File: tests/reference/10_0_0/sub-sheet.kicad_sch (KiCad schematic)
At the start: 1 part, among them U1 74LS04

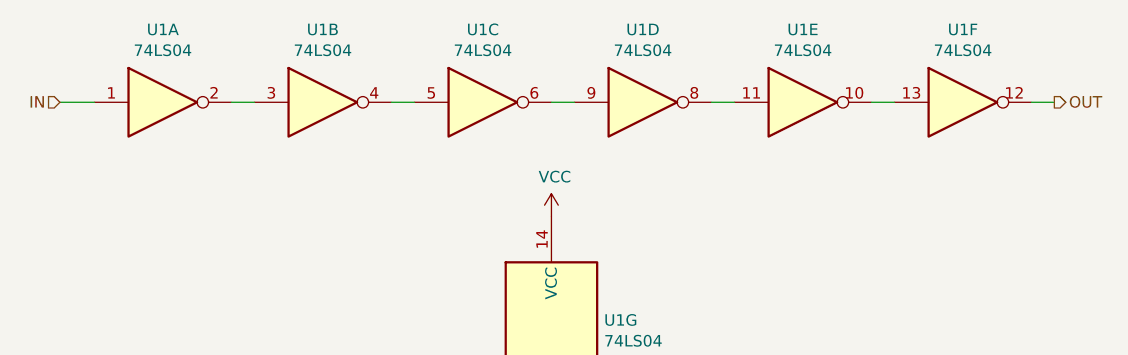
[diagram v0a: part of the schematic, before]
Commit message: [Schematic][Added] Support for private texts on symbols
- Introduced in KiCad 9
- Not documented, as usual
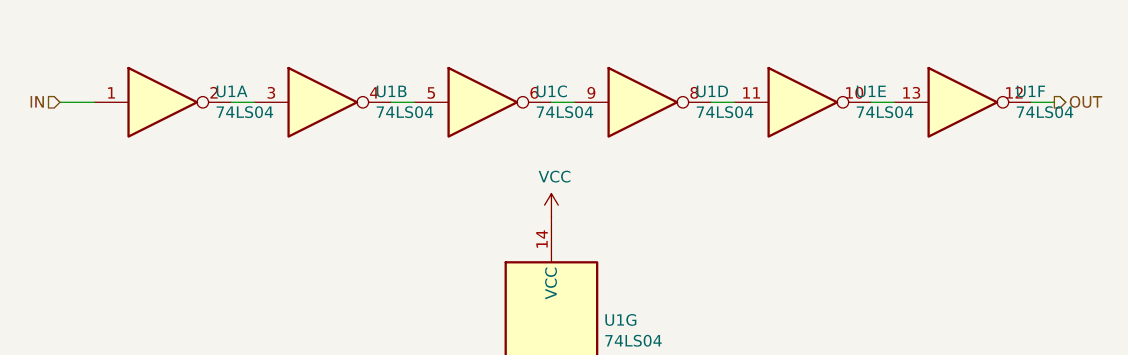
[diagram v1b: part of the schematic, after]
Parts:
- U1: private (none) -> PrivateField
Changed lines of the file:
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@@
-(kicad_sch (version 20260101) (generator "eeschema") (generator_version "10.0")
+(kicad_sch (version 20260306) (generator "eeschema") (generator_version "10.0")
   (paper "User" 297.002 210.007)
   (title_block
@@
     (effects (font (size 1.27 1.27)) (justify left))
   )
-  (symbol (lib_id "74xx:74LS04") (at 96.52 63.5 0) (unit 1) (body_style 1)
-    (exclude_from_sim no) (in_bom yes) (on_board yes) (in_pos_files yes) (dnp no)
-    (property "Reference" "U1" (at 96.52 55.4482 0) (do_not_autoplace no) (show_name no)
-      (effects (font (size 1.27 1.27)))
-    )
-    (property "Value" "74LS04" (at 96.52 57.7596 0) (do_not_autoplace no) (show_name no)
-      (effects (font (size 1.27 1.27)))
+  (symbol (lib_name "74LS04_1") (lib_id "74xx:74LS04") (at 96.52 63.5 0) (unit 1) (body_style 1)
+    (exclude_from_sim no) (in_bom yes) (on_board yes) (in_pos_files yes) (dnp no)
+    (property "Reference" "U1" (at 102.362 62.3316 0) (do_not_autoplace no) (show_name no)
+      (effects (font (size 1.27 1.27)) (justify left))
+    )
+    (property "Value" "74LS04" (at 102.362 64.643 0) (do_not_autoplace no) (show_name no)
+      (effects (font (size 1.27 1.27)) (justify left))
     )
     (property "Footprint" "" (at 96.52 63.5 0) (do_not_autoplace no) (show_name no) (hide yes)
@@
       (effects (font (size 1.27 1.27)))
     )
+    (property private "PrivateField" "Testing 1 2 3" (at 96.52 63.5 0) (do_not_autoplace no) (show_name no) (hide yes)
+      (effects (font (size 1.27 1.27)))
+    )
     (pin "1")
     (pin "2")
@@
     )
   )
-  (symbol (lib_id "74xx:74LS04") (at 114.3 63.5 0) (unit 2) (body_style 1)
-    (exclude_from_sim no) (in_bom yes) (on_board yes) (in_pos_files yes) (dnp no)
-    (property "Reference" "U1" (at 114.3 55.4482 0) (do_not_autoplace no) (show_name no)
-      (effects (font (size 1.27 1.27)))
-    )
-    (property "Value" "74LS04" (at 114.3 57.7596 0) (do_not_autoplace no) (show_name no)
-      (effects (font (size 1.27 1.27)))
+  (symbol (lib_name "74LS04_2") (lib_id "74xx:74LS04") (at 114.3 63.5 0) (unit 2) (body_style 1)
+    (exclude_from_sim no) (in_bom yes) (on_board yes) (in_pos_files yes) (dnp no)
+    (property "Reference" "U1" (at 120.142 62.3316 0) (do_not_autoplace no) (show_name no)
+      (effects (font (size 1.27 1.27)) (justify left))
+    )
+    (property "Value" "74LS04" (at 120.142 64.643 0) (do_not_autoplace no) (show_name no)
+      (effects (font (size 1.27 1.27)) (justify left))
     )
     (property "Footprint" "" (at 114.3 63.5 0) (do_not_autoplace no) (show_name no) (hide yes)
@@
       (effects (font (size 1.27 1.27)))
     )
+    (property private "PrivateField" "Testing 1 2 3" (at 114.3 63.5 0) (do_not_autoplace no) (show_name no) (hide yes)
+      (effects (font (size 1.27 1.27)))
+    )
     (pin "1")
     (pin "2")
@@
     )
   )
-  (symbol (lib_id "74xx:74LS04") (at 132.08 63.5 0) (unit 3) (body_style 1)
-    (exclude_from_sim no) (in_bom yes) (on_board yes) (in_pos_files yes) (dnp no)
-    (property "Reference" "U1" (at 132.08 55.4482 0) (do_not_autoplace no) (show_name no)
-      (effects (font (size 1.27 1.27)))
-    )
-    (property "Value" "74LS04" (at 132.08 57.7596 0) (do_not_autoplace no) (show_name no)
-      (effects (font (size 1.27 1.27)))
+  (symbol (lib_name "74LS04_3") (lib_id "74xx:74LS04") (at 132.08 63.5 0) (unit 3) (body_style 1)
+    (exclude_from_sim no) (in_bom yes) (on_board yes) (in_pos_files yes) (dnp no)
+    (property "Reference" "U1" (at 137.922 62.3316 0) (do_not_autoplace no) (show_name no)
+      (effects (font (size 1.27 1.27)) (justify left))
+    )
+    (property "Value" "74LS04" (at 137.922 64.643 0) (do_not_autoplace no) (show_name no)
+      (effects (font (size 1.27 1.27)) (justify left))
     )
     (property "Footprint" "" (at 132.08 63.5 0) (do_not_autoplace no) (show_name no) (hide yes)
@@
       (effects (font (size 1.27 1.27)))
     )
+    (property private "PrivateField" "Testing 1 2 3" (at 132.08 63.5 0) (do_not_autoplace no) (show_name no) (hide yes)
+      (effects (font (size 1.27 1.27)))
+    )
     (pin "1")
     (pin "2")
@@
     )
   )
-  (symbol (lib_id "74xx:74LS04") (at 149.86 63.5 0) (unit 4) (body_style 1)
-    (exclude_from_sim no) (in_bom yes) (on_board yes) (in_pos_files yes) (dnp no)
-    (property "Reference" "U1" (at 149.86 55.4482 0) (do_not_autoplace no) (show_name no)
-      (effects (font (size 1.27 1.27)))
-    )
-    (property "Value" "74LS04" (at 149.86 57.7596 0) (do_not_autoplace no) (show_name no)
-      (effects (font (size 1.27 1.27)))
+  (symbol (lib_name "74LS04_6") (lib_id "74xx:74LS04") (at 149.86 63.5 0) (unit 4) (body_style 1)
+    (exclude_from_sim no) (in_bom yes) (on_board yes) (in_pos_files yes) (dnp no)
+    (property "Reference" "U1" (at 155.702 62.3316 0) (do_not_autoplace no) (show_name no)
+      (effects (font (size 1.27 1.27)) (justify left))
+    )
+    (property "Value" "74LS04" (at 155.702 64.643 0) (do_not_autoplace no) (show_name no)
+      (effects (font (size 1.27 1.27)) (justify left))
     )
     (property "Footprint" "" (at 149.86 63.5 0) (do_not_autoplace no) (show_name no) (hide yes)
@@
       (effects (font (size 1.27 1.27)))
     )
+    (property private "PrivateField" "Testing 1 2 3" (at 149.86 63.5 0) (do_not_autoplace no) (show_name no) (hide yes)
+      (effects (font (size 1.27 1.27)))
+    )
     (pin "1")
     (pin "2")
@@
     )
   )
-  (symbol (lib_id "74xx:74LS04") (at 167.64 63.5 0) (unit 5) (body_style 1)
-    (exclude_from_sim no) (in_bom yes) (on_board yes) (in_pos_files yes) (dnp no)
-    (property "Reference" "U1" (at 167.64 55.4482 0) (do_not_autoplace no) (show_name no)
-      (effects (font (size 1.27 1.27)))
-    )
-    (property "Value" "74LS04" (at 167.64 57.7596 0) (do_not_autoplace no) (show_name no)
-      (effects (font (size 1.27 1.27)))
+  (symbol (lib_name "74LS04_5") (lib_id "74xx:74LS04") (at 167.64 63.5 0) (unit 5) (body_style 1)
+    (exclude_from_sim no) (in_bom yes) (on_board yes) (in_pos_files yes) (dnp no)
+    (property "Reference" "U1" (at 173.482 62.3316 0) (do_not_autoplace no) (show_name no)
+      (effects (font (size 1.27 1.27)) (justify left))
+    )
+    (property "Value" "74LS04" (at 173.482 64.643 0) (do_not_autoplace no) (show_name no)
+      (effects (font (size 1.27 1.27)) (justify left))
     )
     (property "Footprint" "" (at 167.64 63.5 0) (do_not_autoplace no) (show_name no) (hide yes)
@@
       (effects (font (size 1.27 1.27)))
     )
+    (property private "PrivateField" "Testing 1 2 3" (at 167.64 63.5 0) (do_not_autoplace no) (show_name no) (hide yes)
+      (effects (font (size 1.27 1.27)))
+    )
     (pin "1")
     (pin "2")
@@
     )
   )
-  (symbol (lib_id "74xx:74LS04") (at 185.42 63.5 0) (unit 6) (body_style 1)
-    (exclude_from_sim no) (in_bom yes) (on_board yes) (in_pos_files yes) (dnp no)
-    (property "Reference" "U1" (at 185.42 55.4482 0) (do_not_autoplace no) (show_name no)
-      (effects (font (size 1.27 1.27)))
-    )
-    (property "Value" "74LS04" (at 185.42 57.7596 0) (do_not_autoplace no) (show_name no)
-      (effects (font (size 1.27 1.27)))
+  (symbol (lib_name "74LS04_4") (lib_id "74xx:74LS04") (at 185.42 63.5 0) (unit 6) (body_style 1)
+    (exclude_from_sim no) (in_bom yes) (on_board yes) (in_pos_files yes) (dnp no)
+    (property "Reference" "U1" (at 191.262 62.3316 0) (do_not_autoplace no) (show_name no)
+      (effects (font (size 1.27 1.27)) (justify left))
+    )
+    (property "Value" "74LS04" (at 191.262 64.643 0) (do_not_autoplace no) (show_name no)
+      (effects (font (size 1.27 1.27)) (justify left))
     )
     (property "Footprint" "" (at 185.42 63.5 0) (do_not_autoplace no) (show_name no) (hide yes)
@@
       (effects (font (size 1.27 1.27)))
     )
+    (property private "PrivateField" "Testing 1 2 3" (at 185.42 63.5 0) (do_not_autoplace no) (show_name no) (hide yes)
+      (effects (font (size 1.27 1.27)))
+    )
     (pin "1")
     (pin "2")
@@
       (effects (font (size 1.27 1.27)))
     )
+    (property private "PrivateField" "Testing 1 2 3" (at 139.7 88.9 0) (do_not_autoplace no) (show_name no) (hide yes)
+      (effects (font (size 1.27 1.27)))
+    )
